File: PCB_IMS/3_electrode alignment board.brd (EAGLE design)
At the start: 104.4 x 48.3 mm, 60 parts

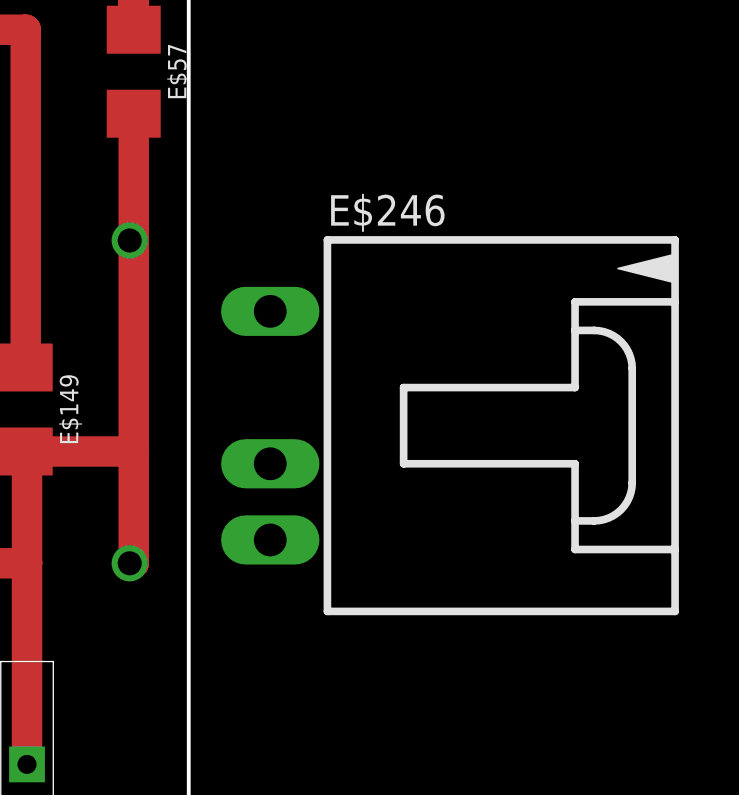
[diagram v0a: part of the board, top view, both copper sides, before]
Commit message: Included slot library
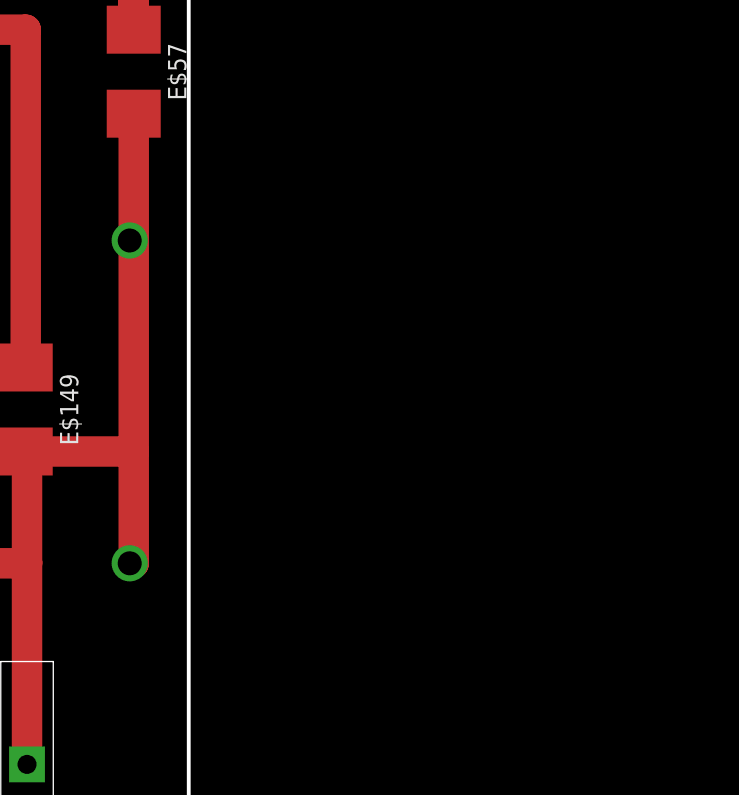
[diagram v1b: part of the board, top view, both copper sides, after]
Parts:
- removed E$246: (no value), GAAextensions:70553-04-NO2
- E$1, E$10, E$11, E$12, E$13, E$14, E$15, E$16, E$17, E$18, E$19, E$2, E$20, E$21, E$22, E$23, E$24, E$25, E$26, E$27, E$28, E$29, E$3, E$4, E$5, E$6, E$7, E$8, E$9: device CouplerDC:GAAEXTENSIONS_SLOT2 -> CouplerDC:SLOT2
